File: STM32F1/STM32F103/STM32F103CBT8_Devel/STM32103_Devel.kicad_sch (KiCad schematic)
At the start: 15 parts, among them J4 Conn_01x16, J5 Conn_01x16, U2 AMS1117-3.3

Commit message: MPN from 030
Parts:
- C10, C14: LCSC C7171 -> C7171; Manufacturer (none) -> Kemet; mnp (none) -> T491A106K010AT
- D1: LCSC C84256 -> C84256; Manufacturer (none) -> Würth Elektronik; mnp (none) -> 150080RS75000
- D2: Manufacturer (none) -> Würth Elektronik; mnp (none) -> 150080BS75000
- D3: Manufacturer (none) -> Würth Elektronik; mnp (none) -> 150080GS75000
- R2: LCSC C17414 -> C17414; Manufacturer (none) -> Bourns Inc.; mnp (none) -> CR0805-FX-1002ELF
- R4, R6: LCSC C17513 -> C17513; Manufacturer (none) -> Bourns Inc.; mnp (none) -> CR0805-FX-1001ELF
- U2: LCSC C6186 -> C6186

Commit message: Mpn ids
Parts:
- U2: Manufacturer (none) -> EVVO; mnp (none) -> AMS1117-3.3
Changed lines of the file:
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@@
 			)
 		)
-		(property "Manufacturer" ""
+		(property "Manufacturer" "EVVO"
 			(at 228.6 121.92 0)
 			(effects
@@
 			)
 		)
-		(property "mnp" ""
+		(property "mnp" "AMS1117-3.3"
 			(at 228.6 121.92 0)
 			(effects

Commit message: Mov USB
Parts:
- H1, H2, H3, H4: footprint MountingHole:MountingHole_2.7mm_M2.5 -> MountingHole:MountingHole_2.7mm_M2.5_DIN965_Pad; symbol Mechanical:MountingHole -> Mechanical:MountingHole_Pad; now left out of the parts list
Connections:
- net GND: now also H1.1, H2.1, H3.1, H4.1
- no-connect marks 1 -> 7

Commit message: Power Buttons
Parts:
- added J1, J3: Conn_02x03_Counter_Clockwise, Connector_PinHeader_2.54mm:PinHeader_2x03_P2.54mm_Vertical, symbol Connector_Generic:Conn_02x03_Odd_Even
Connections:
- net +5V: now also J3.1 (Pin_1), J3.3 (Pin_3), J3.5 (Pin_5)
- net GND: now also J1.2 (Pin_2), J1.4 (Pin_4), J1.6 (Pin_6), J3.2 (Pin_2), J3.4 (Pin_4), J3.6 (Pin_6)
- net VCC: now also J1.1 (Pin_1), J1.3 (Pin_3), J1.5 (Pin_5)

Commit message: MPN
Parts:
- C10, C14: mnp T491A106K010AT -> (none); mpn (none) -> T491A106K010AT
- D1: mnp 150080RS75000 -> (none); mpn (none) -> 150080RS75000
- D2: mnp 150080BS75000 -> (none); mpn (none) -> 150080BS75000
- D3: mnp 150080GS75000 -> (none); mpn (none) -> 150080GS75000
- R2: mnp CR0805-FX-1002ELF -> (none); mpn (none) -> CR0805-FX-1002ELF
- R4, R6: mnp CR0805-FX-1001ELF -> (none); mpn (none) -> CR0805-FX-1001ELF
- U2: mnp AMS1117-3.3 -> (none); mpn (none) -> AMS1117-3.3
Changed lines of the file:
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@@
 			)
 		)
-		(property "mnp" "AMS1117-3.3"
+		(property "mpn" "AMS1117-3.3"
 			(at 228.6 121.92 0)
 			(effects
@@
 			)
 		)
-		(property "mnp" "T491A106K010AT"
+		(property "mpn" "T491A106K010AT"
 			(at 248.92 127 0)
 			(effects
@@
 			)
 		)
-		(property "mnp" "T491A106K010AT"
+		(property "mpn" "T491A106K010AT"
 			(at 213.36 127 0)
 			(effects
@@
 			)
 		)
-		(property "mnp" ""
-			(at 238.76 22.86 0)
-			(effects
-				(font
-					(size 1.27 1.27)
-				)
-				(hide yes)
-			)
-		)
 		(pin "1"
 		)
@@
 			)
 		)
-		(property "mnp" ""
-			(at 256.54 22.86 0)
-			(effects
-				(font
-					(size 1.27 1.27)
-				)
-				(hide yes)
-			)
-		)
 		(pin "1"
 		)
@@
 			)
 		)
-		(property "mnp" ""
-			(at 238.76 34.29 0)
-			(effects
-				(font
-					(size 1.27 1.27)
-				)
-				(hide yes)
-			)
-		)
 		(pin "1"
 		)
@@
 		)
 		(property "Manufacturer" ""
-			(at 256.54 34.29 0)
-			(effects
-				(font
-					(size 1.27 1.27)
-				)
-				(hide yes)
-			)
-		)
-		(property "mnp" ""
 			(at 256.54 34.29 0)
 			(effects
@@
 			)
 		)
-		(property "mnp" ""
-			(at 57.15 121.92 0)
-			(effects
-				(font
-					(size 1.27 1.27)
-				)
-				(hide yes)
-			)
-		)
 		(pin "1"
 		)
@@
 			)
 		)
-		(property "mnp" ""
-			(at 46.99 121.92 0)
-			(effects
-				(font
-					(size 1.27 1.27)
-				)
-				(hide yes)
-			)
-		)
 		(pin "1"
 		)
@@
 			)
 		)
-		(property "mnp" "CR0805-FX-1001ELF"
+		(property "mpn" "CR0805-FX-1001ELF"
 			(at 182.88 39.37 0)
 			(effects
@@
 			)
 		)
-		(property "mnp" "150080RS75000"
+		(property "mpn" "150080RS75000"
 			(at 172.72 50.8 0)
 			(effects
@@
 			)
 		)
-		(property "mnp" "150080BS75000"
+		(property "mpn" "150080BS75000"
 			(at 182.88 50.8 0)
 			(effects
@@
 			)
 		)
-		(property "mnp" "CR0805-FX-1002ELF"
+		(property "mpn" "CR0805-FX-1002ELF"
 			(at 172.72 39.37 0)
 			(effects
@@
 			)
 		)
-		(property "mnp" "CR0805-FX-1001ELF"
+		(property "mpn" "CR0805-FX-1001ELF"
 			(at 191.77 39.37 0)
 			(effects
@@
 			)
 		)
-		(property "mnp" "150080GS75000"
+		(property "mpn" "150080GS75000"
 			(at 191.77 50.8 0)
 			(effects

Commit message: Changes
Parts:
- J1, J3: LCSC (none) -> C2685197; Manufacturer (none) -> Adam Tech; mpn (none) -> PH2-06-UA
- J4, J5: LCSC (none) -> C7430372; Manufacturer (none) -> Adam Tech; mpn (none) -> PH1-16-UA
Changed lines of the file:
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@@
 			)
 		)
-		(property "Manufacturer" ""
+		(property "Manufacturer" "Adam Tech"
+			(at 57.15 121.92 0)
+			(effects
+				(font
+					(size 1.27 1.27)
+				)
+				(hide yes)
+			)
+		)
+		(property "mpn" "PH1-16-UA"
+			(at 57.15 121.92 0)
+			(effects
+				(font
+					(size 1.27 1.27)
+				)
+				(hide yes)
+			)
+		)
+		(property "LCSC" "C7430372"
 			(at 57.15 121.92 0)
 			(effects
@@
 			)
 		)
-		(property "Manufacturer" ""
+		(property "Manufacturer" "Adam Tech"
+			(at 46.99 121.92 0)
+			(effects
+				(font
+					(size 1.27 1.27)
+				)
+				(hide yes)
+			)
+		)
+		(property "mpn" "PH1-16-UA"
+			(at 46.99 121.92 0)
+			(effects
+				(font
+					(size 1.27 1.27)
+				)
+				(hide yes)
+			)
+		)
+		(property "LCSC" "C7430372"
 			(at 46.99 121.92 0)
 			(effects
@@
 			)
 		)
+		(property "Manufacturer" "Adam Tech"
+			(at 135.89 119.38 0)
+			(effects
+				(font
+					(size 1.27 1.27)
+				)
+				(hide yes)
+			)
+		)
+		(property "mpn" "PH2-06-UA"
+			(at 135.89 119.38 0)
+			(effects
+				(font
+					(size 1.27 1.27)
+				)
+				(hide yes)
+			)
+		)
+		(property "LCSC" "C2685197"
+			(at 135.89 119.38 0)
+			(effects
+				(font
+					(size 1.27 1.27)
+				)
+				(hide yes)
+			)
+		)
 		(pin "4"
 		)
@@
 			(at 135.89 96.52 0)
 			(effects
+				(font
+					(size 1.27 1.27)
+				)
+				(hide yes)
+			)
+		)
+		(property "Manufacturer" "Adam Tech"
+			(at 135.89 96.52 0)
+			(effects
+				(font
+					(size 1.27 1.27)
+				)
+				(hide yes)
+			)
+		)
+		(property "mpn" "PH2-06-UA"
+			(at 135.89 96.52 0)
+			(effects
+				(font
+					(size 1.27 1.27)
+				)
+				(hide yes)
+			)
+		)
+		(property "LCSC" "C2685197"
+			(at 135.89 96.52 0)
+			(effects

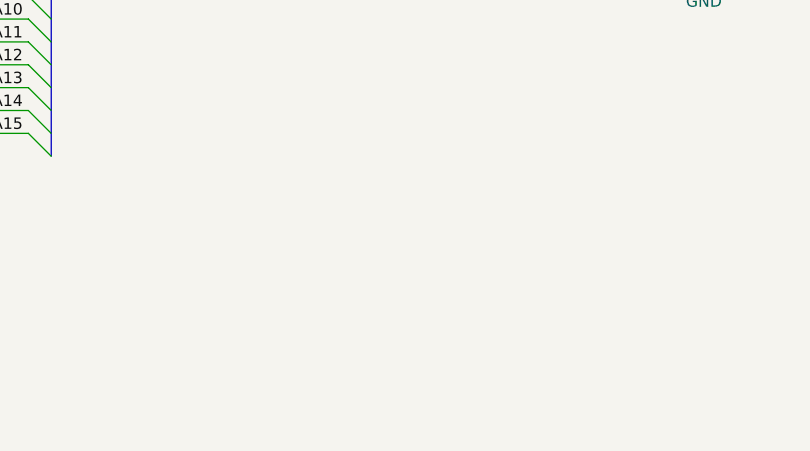
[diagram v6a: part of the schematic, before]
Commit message: I2C pull-Up
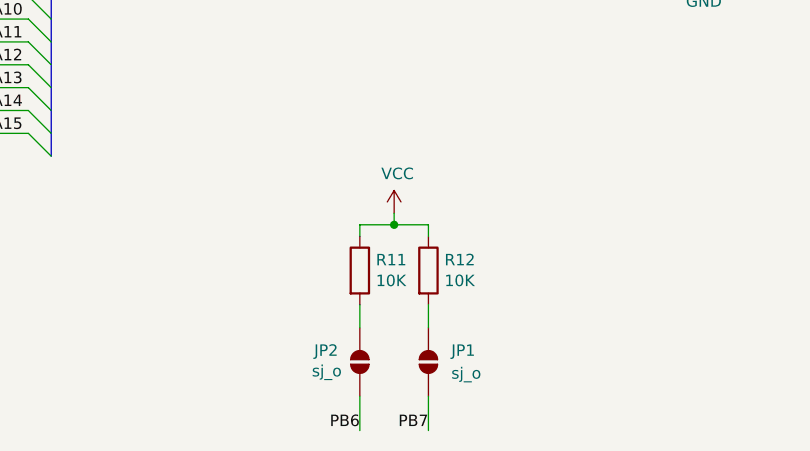
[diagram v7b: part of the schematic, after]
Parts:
- added JP1, JP2: sj_o, Jumper:SolderJumper-2_P1.3mm_Open_TrianglePad1.0x1.5mm, symbol Jumper:SolderJumper_2_Open
- added R11, R12: 10K, Resistor_SMD:R_0805_2012Metric, symbol Device:R
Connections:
- net PB6: now also JP2.1 (A)
- net PB7: now also JP1.1 (A)
- net VCC: now also R11.1, R12.1
- new net: JP1.2 (B), R12.2
- new net: JP2.2 (B), R11.2

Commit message: Doc updated
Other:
- company: (none) -> Daniel Vilas
- title: (none) -> STM32F103 Devel
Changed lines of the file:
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@@
 	(paper "A4")
 	(title_block
-		(date "2020-07-01")
-		(rev "0.0.2")
+		(title "STM32F103 Devel")
+		(date "2024-08-19")
+		(rev "0.0.3")
+		(company "Daniel Vilas")
 	)
 	(junction
